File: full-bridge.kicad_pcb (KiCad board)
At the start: 2 copper layers, 14 parts, among them U801 VNH7070ASTR

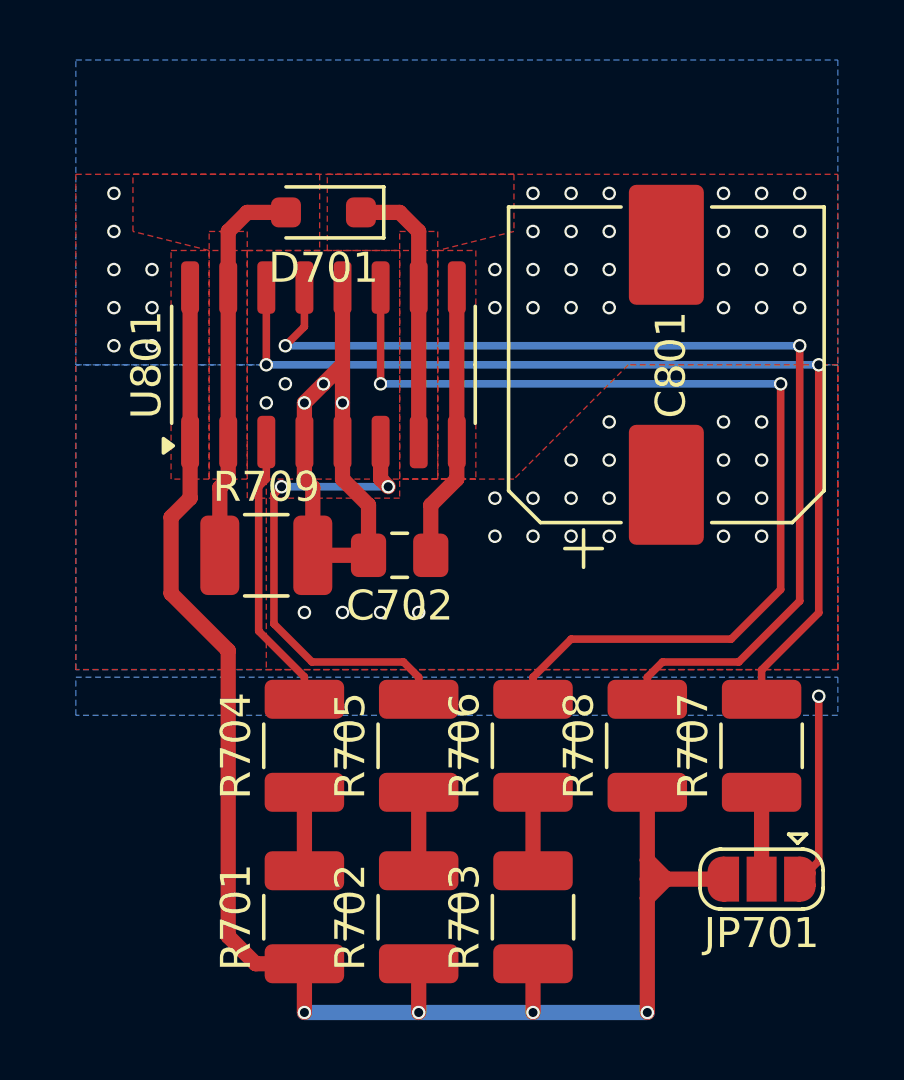
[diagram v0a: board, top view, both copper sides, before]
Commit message: ajust output channel order
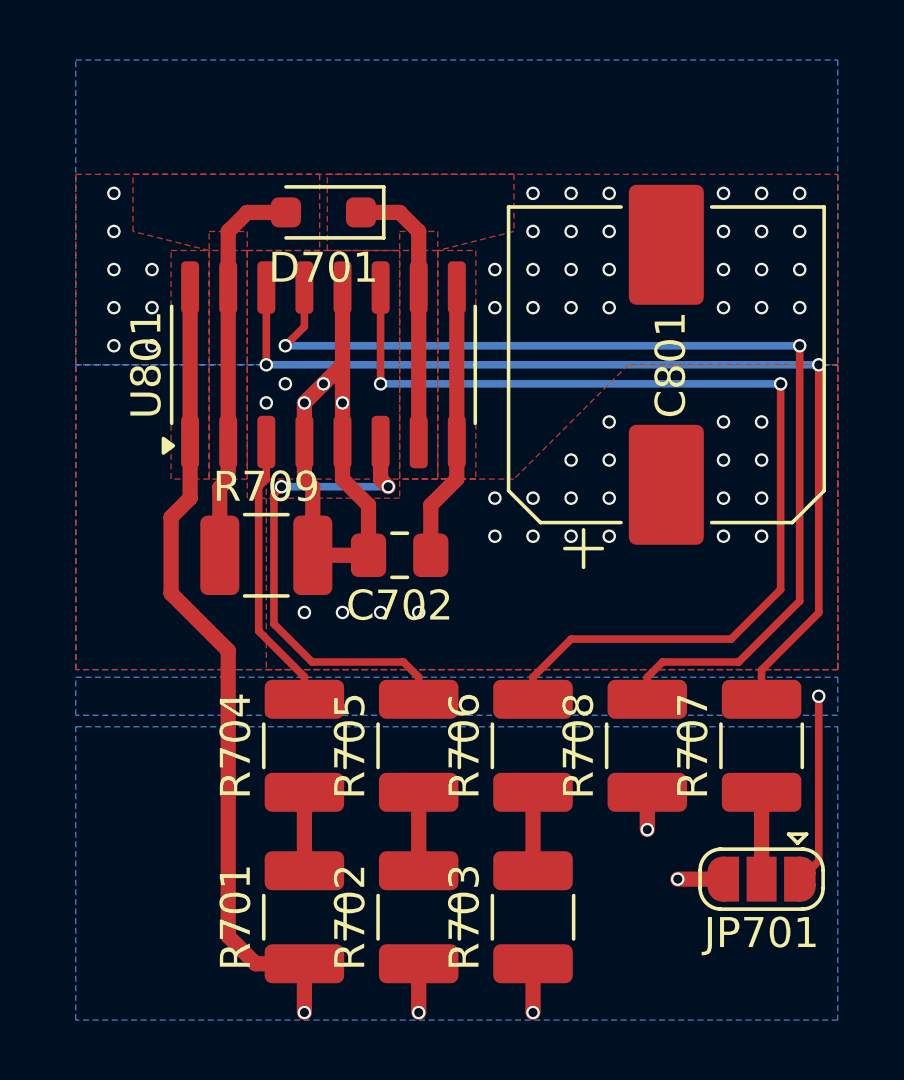
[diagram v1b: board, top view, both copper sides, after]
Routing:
- net GND: track 62.8 -> 42.5 mm, vias 38 -> 39
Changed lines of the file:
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@@
 		(tags "resistor handsolder")
 		(property "Reference" "R704"
-			(at 0 -2.28 270)
+			(at 0 -2.28 -90)
 			(layer "F.SilkS")
 			(effects
@@
 		)
 		(property "Value" "1k"
-			(at 0 2.28 270)
+			(at 0 2.28 -90)
 			(layer "F.Fab")
 			(effects
@@
 		)
 		(fp_text user "${REFERENCE}"
-			(at 0 0 270)
+			(at 0 0 -90)
 			(layer "F.Fab")
 			(effects
@@
 		(tags "resistor handsolder")
 		(property "Reference" "R706"
-			(at 0 -2.28 270)
+			(at 0 -2.28 -90)
 			(layer "F.SilkS")
 			(effects
@@
 		)
 		(property "Value" "1k"
-			(at 0 2.28 270)
+			(at 0 2.28 -90)
 			(layer "F.Fab")
 			(effects
@@
 		)
 		(fp_text user "${REFERENCE}"
-			(at 0 0 270)
+			(at 0 0 -90)
 			(layer "F.Fab")
 			(effects
@@
 		(tags "SO SO SOT109-1")
 		(property "Reference" "U801"
-			(at 0 -5.9 270)
+			(at 0 -5.9 -90)
 			(layer "F.SilkS")
 			(effects
@@
 		)
 		(property "Value" "VNH7070ASTR"
-			(at 0 5.9 270)
+			(at 0 5.9 -90)
 			(layer "F.Fab")
 			(effects
@@
 		)
 		(fp_text user "${REFERENCE}"
-			(at 0 0 270)
+			(at 0 0 -90)
 			(layer "F.Fab")
 			(effects
@@
 		(tags "resistor handsolder")
 		(property "Reference" "R708"
-			(at 0 -2.28 270)
+			(at 0 -2.28 -90)
 			(layer "F.SilkS")
 			(effects
@@
 		)
 		(property "Value" "1k"
-			(at 0 2.28 270)
+			(at 0 2.28 -90)
 			(layer "F.Fab")
 			(effects
@@
 		)
 		(fp_text user "${REFERENCE}"
-			(at 0 0 270)
+			(at 0 0 -90)
 			(layer "F.Fab")
 			(effects
@@
 		(tags "resistor handsolder")
 		(property "Reference" "R703"
-			(at 0 -2.28 270)
+			(at 0 -2.28 -90)
 			(layer "F.SilkS")
 			(effects
@@
 		)
 		(property "Value" "1M"
-			(at 0 2.28 270)
+			(at 0 2.28 -90)
 			(layer "F.Fab")
 			(effects
@@
 		)
 		(fp_text user "${REFERENCE}"
-			(at 0 0 270)
+			(at 0 0 -90)
 			(layer "F.Fab")
 			(effects
@@
 		(tags "resistor handsolder")
 		(property "Reference" "R705"
-			(at 0 -2.28 270)
+			(at 0 -2.28 -90)
 			(layer "F.SilkS")
 			(effects
@@
 		)
 		(property "Value" "1k"
-			(at 0 2.28 270)
+			(at 0 2.28 -90)
 			(layer "F.Fab")
 			(effects
@@
 		)
 		(fp_text user "${REFERENCE}"
-			(at 0 0 270)
+			(at 0 0 -90)
 			(layer "F.Fab")
 			(effects
@@
 		(tags "capacitor electrolytic")
 		(property "Reference" "C801"
-			(at 0 0.15 270)
+			(at 0 0.15 -90)
 			(layer "F.SilkS")
 			(effects
@@
 		)
 		(property "Value" "470u"
-			(at 0 3.81 270)
+			(at 0 3.81 -90)
 			(layer "F.Fab")
 			(effects
@@
 		)
 		(fp_text user "${REFERENCE}"
-			(at 0 0 270)
+			(at 0 0 -90)
 			(layer "F.Fab")
 			(effects
@@
 		(tags "resistor handsolder")
 		(property "Reference" "R702"
-			(at 0 -2.28 270)
+			(at 0 -2.28 -90)
 			(layer "F.SilkS")
 			(effects
@@
 		)
 		(property "Value" "1M"
-			(at 0 2.28 270)
+			(at 0 2.28 -90)
 			(layer "F.Fab")
 			(effects
@@
 		)
 		(fp_text user "${REFERENCE}"
-			(at 0 0 270)
+			(at 0 0 -90)
 			(layer "F.Fab")
 			(effects
@@
 		(tags "resistor handsolder")
 		(property "Reference" "R701"
-			(at 0 -2.28 270)
+			(at 0 -2.28 -90)
 			(layer "F.SilkS")
 			(effects
@@
 		)
 		(property "Value" "1M"
-			(at 0 2.28 270)
+			(at 0 2.28 -90)
 			(layer "F.Fab")
 			(effects
@@
 		)
 		(fp_text user "${REFERENCE}"
-			(at 0 0 270)
+			(at 0 0 -90)
 			(layer "F.Fab")
 			(effects
@@
 		(tags "resistor handsolder")
 		(property "Reference" "R707"
-			(at 0 -2.28 270)
+			(at 0 -2.28 -90)
 			(layer "F.SilkS")
 			(effects
@@
 		)
 		(property "Value" "1k"
-			(at 0 2.28 270)
+			(at 0 2.28 -90)
 			(layer "F.Fab")
 			(effects
@@
 		)
 		(fp_text user "${REFERENCE}"
-			(at 0 0 270)
+			(at 0 0 -90)
 			(layer "F.Fab")
 			(effects
@@
 	)
 	(segment
-		(start 63.5 54.575)
-		(end 63.5 59.725)
+		(start 72.36 74.295)
+		(end 70.866 74.295)
 		(width 0.508)
 		(layer "F.Cu")
@@
 	)
 	(segment
-		(start 72.36 74.295)
-		(end 70.485 74.295)
+		(start 63.5 54.575)
+		(end 63.5 59.725)
 		(width 0.508)
 		(layer "F.Cu")
@@
 	)
 	(segment
-		(start 69.85 74.93)
-		(end 69.85 74.295)
+		(start 69.85 71.4)
+		(end 69.85 72.644)
 		(width 0.508)
 		(layer "F.Cu")
@@
 	)
 	(segment
-		(start 70.485 74.295)
-		(end 69.85 74.93)
-		(width 0.508)
-		(layer "F.Cu")
-		(net 1)
-	)
-	(segment
-		(start 70.485 74.295)
-		(end 69.85 74.295)
-		(width 0.508)
-		(layer "F.Cu")
-		(net 1)
-	)
-	(segment
 		(start 53.975 64.77)
 		(end 55.88 66.675)
@@
 	)
 	(segment
-		(start 69.85 78.74)
-		(end 69.85 74.93)
-		(width 0.508)
-		(layer "F.Cu")
-		(net 1)
-	)
-	(segment
 		(start 55.88 66.675)
 		(end 55.88 76.2)
@@
 	)
 	(segment
-		(start 69.85 74.295)
-		(end 69.85 73.66)
-		(width 0.508)
-		(layer "F.Cu")
-		(net 1)
-	)
-	(segment
 		(start 53.975 62.23)
 		(end 53.975 64.77)
@@
 	)
 	(segment
-		(start 69.85 73.66)
-		(end 69.85 71.4)
-		(width 0.508)
-		(layer "F.Cu")
-		(net 1)
-	)
-	(segment
-		(start 70.485 74.295)
-		(end 69.85 73.66)
-		(width 0.508)
-		(layer "F.Cu")
-		(net 1)
-	)
-	(segment
 		(start 54.61 61.595)
 		(end 53.975 62.23)
@@
 	)
 	(via
+		(at 69.85 72.644)
+		(size 0.45)
+		(drill 0.3)
+		(layers "F.Cu" "B.Cu")
+		(net 1)
+	)
+	(via
 		(at 74.93 53.975)
 		(size 0.45)
@@
 	)
 	(via
+		(at 70.866 74.295)
+		(size 0.45)
+		(drill 0.3)
+		(layers "F.Cu" "B.Cu")
+		(net 1)
+	)
+	(via
 		(at 73.66 53.975)
 		(size 0.45)
@@
 	)
 	(via
-		(at 69.85 78.74)
-		(size 0.45)
-		(drill 0.3)
-		(layers "F.Cu" "B.Cu")
-		(net 1)
-	)
-	(via
 		(at 66.04 51.435)
 		(size 0.45)
@@
 	)
 	(segment
-		(start 66.04 78.74)
-		(end 69.85 78.74)
-		(width 0.508)
-		(layer "B.Cu")
-		(net 1)
-	)
-	(segment
-		(start 62.23 78.74)
-		(end 66.04 78.74)
-		(width 0.508)
-		(layer "B.Cu")
-		(net 1)
-	)
-	(segment
-		(start 58.42 78.74)
-		(end 62.23 78.74)
-		(width 0.508)
-		(layer "B.Cu")
-		(net 1)
-	)
-	(segment
 		(start 59.69 57.15)
 		(end 59.69 54.575)
@@
 		(polygon
 			(pts
-				(xy 62.865 53.34) (xy 61.595 53.34) (xy 61.595 53.34) (xy 59.182 53.34) (xy 59.182 50.8) (xy 65.405 50.8)
-				(xy 65.405 52.705) (xy 62.865 53.34)
+				(xy 62.865 53.34) (xy 61.595 53.34) (xy 59.182 53.34) (xy 59.182 50.8) (xy 65.405 50.8) (xy 65.405 52.705)
 			)
 		)
@@
 		(polygon
 			(pts
-				(xy 56.515 53.34) (xy 55.245 53.34) (xy 55.245 53.34) (xy 52.705 52.705) (xy 52.705 50.8) (xy 58.928 50.8)
-				(xy 58.928 53.34) (xy 56.515 53.34)
+				(xy 56.515 53.34) (xy 55.245 53.34) (xy 52.705 52.705) (xy 52.705 50.8) (xy 58.928 50.8) (xy 58.928 53.34)
 			)
 		)
@@
 			)
 		)
+	)
+	(zone
+		(net 1)
+		(net_name "GND")
+		(layer "B.Cu")
+		(hatch edge 0.5)
+		(priority 90)
+		(connect_pads
+			(clearance 0.254)
+		)
+		(min_thickness 0.254)
+		(filled_areas_thickness no)
+		(fill yes
+			(thermal_gap 0.254)
+			(thermal_bridge_width 0.508)
+		)
+		(polygon
+			(pts
+				(xy 50.8 69.215) (xy 76.2 69.215) (xy 76.2 78.994) (xy 50.8 78.994)
+			)
+		)

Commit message: enhance silk screen
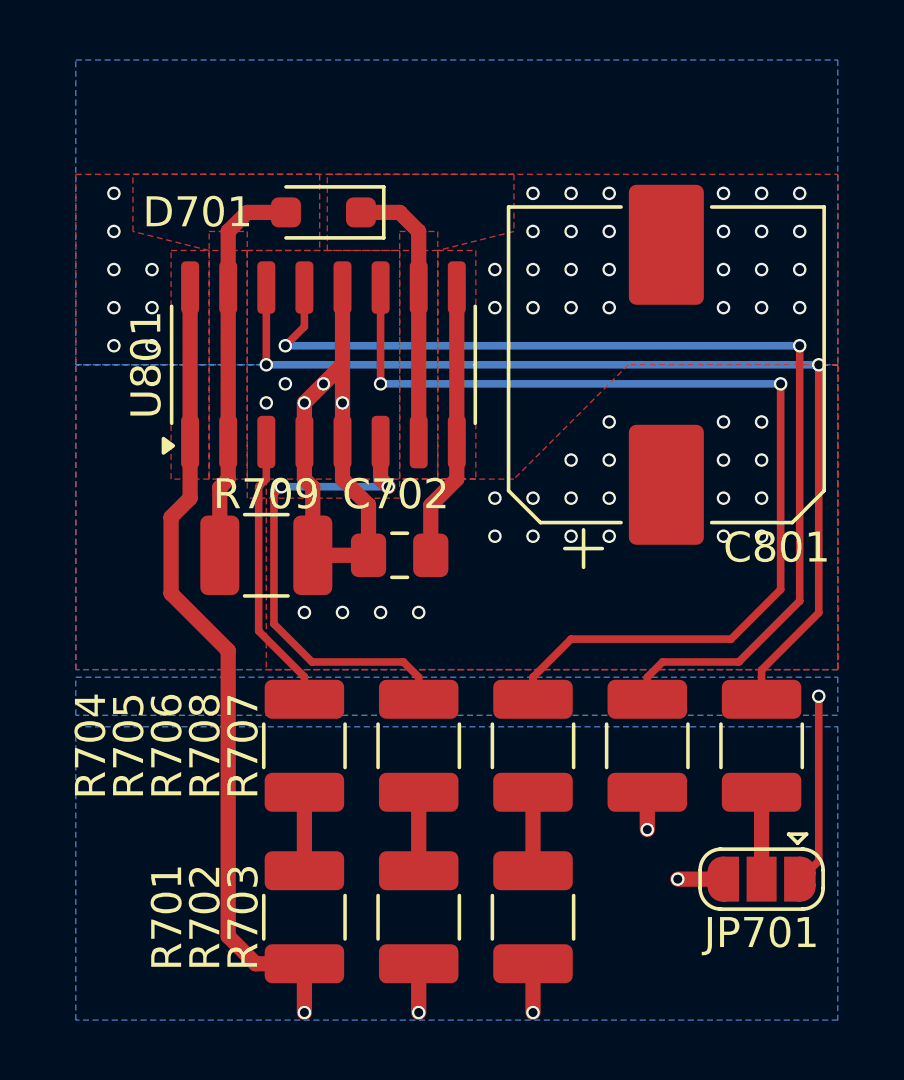
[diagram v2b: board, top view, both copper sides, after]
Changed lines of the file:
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@@
 		(tags "resistor handsolder")
 		(property "Reference" "R704"
-			(at 0 -2.28 -90)
+			(at 0 -7.112 -90)
 			(layer "F.SilkS")
 			(effects
@@
 		(tags "resistor handsolder")
 		(property "Reference" "R706"
-			(at 0 -2.28 -90)
+			(at 0 -12.192 -90)
 			(layer "F.SilkS")
 			(effects
@@
 		(tags "resistor handsolder")
 		(property "Reference" "R708"
-			(at 0 -2.28 -90)
+			(at 0 -14.732 -90)
 			(layer "F.SilkS")
 			(effects
@@
 		(tags "resistor handsolder")
 		(property "Reference" "R703"
-			(at 0 -2.28 -90)
+			(at 0 -9.652 -90)
 			(layer "F.SilkS")
 			(effects
@@
 		(tags "resistor handsolder")
 		(property "Reference" "R705"
-			(at 0 -2.28 -90)
+			(at 0 -9.652 -90)
 			(layer "F.SilkS")
 			(effects
@@
 		(tags "capacitor electrolytic")
 		(property "Reference" "C801"
-			(at 0 0.15 -90)
+			(at -6.096 3.683 0)
 			(layer "F.SilkS")
 			(effects
@@
 		(tags "resistor handsolder")
 		(property "Reference" "R702"
-			(at 0 -2.28 -90)
+			(at 0 -7.112 -90)
 			(layer "F.SilkS")
 			(effects
@@
 		(tags "SOD-323")
 		(property "Reference" "D701"
-			(at 0 -1.85 180)
+			(at 4.191 0 180)
 			(layer "F.SilkS")
 			(effects
@@
 		(tags "capacitor handsolder")
 		(property "Reference" "C702"
-			(at 0 -1.68 180)
+			(at 0.127 2.032 180)
 			(layer "F.SilkS")
 			(effects
@@
 		(tags "resistor handsolder")
 		(property "Reference" "R701"
-			(at 0 -2.28 -90)
+			(at 0 -4.572 -90)
 			(layer "F.SilkS")
 			(effects
@@
 		(tags "resistor handsolder")
 		(property "Reference" "R707"
-			(at 0 -2.28 -90)
+			(at 0 -17.272 -90)
 			(layer "F.SilkS")
 			(effects
@@
 		(tags "resistor handsolder")
 		(property "Reference" "R709"
-			(at 0 -2.28 0)
+			(at 0 -2.032 0)
 			(layer "F.SilkS")
 			(effects
